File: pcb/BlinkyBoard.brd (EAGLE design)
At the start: 25.2 x 10 mm, 27 parts, among them Q1 16 MHz

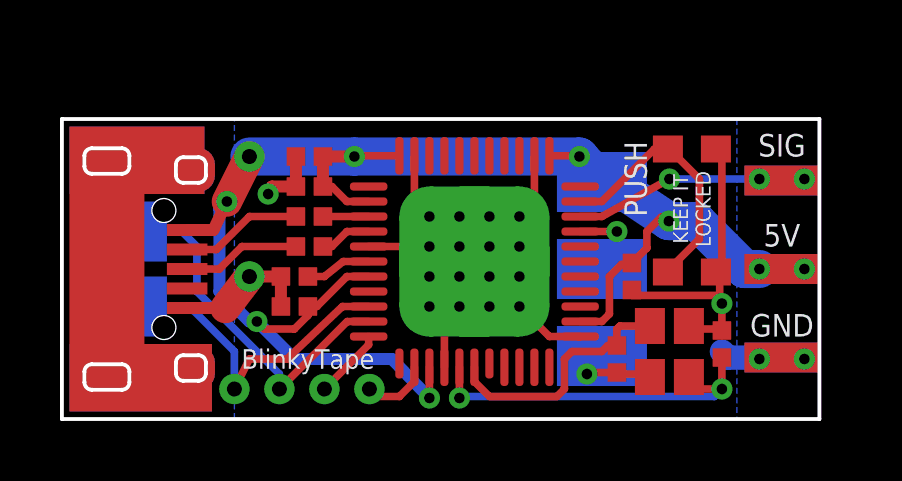
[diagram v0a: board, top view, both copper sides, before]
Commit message: Fix thru-hole micro usb pads, switch 10uF cap to 0603 package
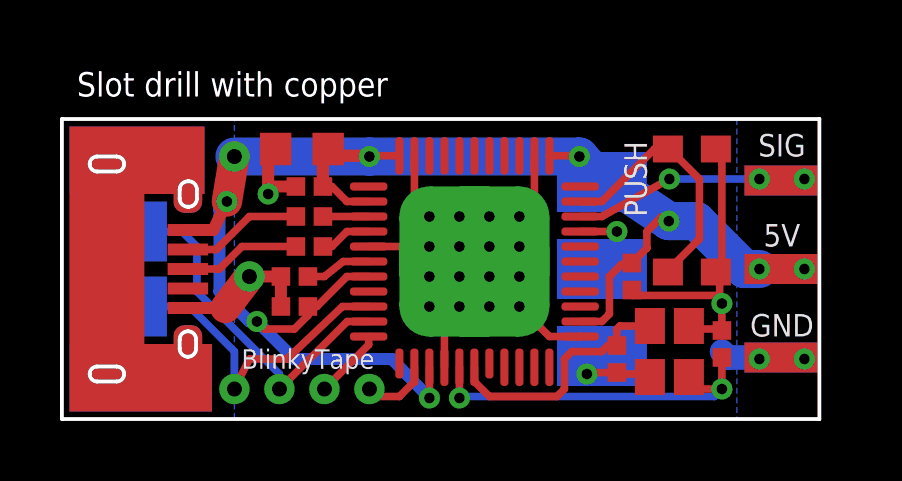
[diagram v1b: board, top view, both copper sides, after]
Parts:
- C1: device blinkiverse:CAP_0402_KEMET_MEDIAN -> adafruit:C0603K
- U$4: value MICRO_USBSMT+DIP -> MICRO_USBSMT+THRUHULE; device blinkiverse:MICRO_USB_THRUHOLE -> blinkiverse:MICRO_USB_FCI_THRUHOLE
- moved U$8 0.50 mm to (5.75, 8.75)
- moved C1 0.35 mm to (8.00, 9.00)
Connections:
- net D+_IN: now also U$4.PIN$3; no longer U$4.P$3
- net D-_IN: now also U$4.PIN$2; no longer U$4.P$2
- net GND: now also C1.2, U$4.PIN$5; no longer C1.P$2, U$4.P$5
- net VCC: now also C1.1, U$4.PIN$1; no longer C1.P$1, U$4.P$1
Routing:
- net VCC: track 54.2 -> 55.0 mm
- net GND: track 33.4 -> 34.2 mm
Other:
- board text added: "Slot drill with copper"
- board text removed: "KEEP IT LOCKED"

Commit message: Swap extra IO pads for ones that are actually Arduino pins, rename analog to A11
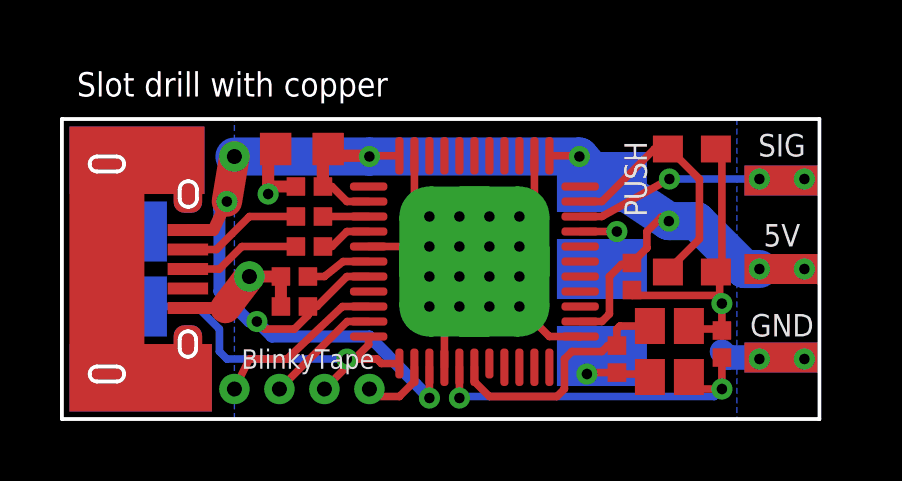
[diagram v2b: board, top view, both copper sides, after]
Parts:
- moved U$10 2.50 mm to (2.00, 6.25)
- moved U$14 2.50 mm to (2.00, 3.75)
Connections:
- net ANALOG_IN renamed A11
- new net D11: U$14.P$1, U$2.12
- new net D7: U$10.P$1, U$2.1
- net MOSI: no longer U$14.P$1
- net SCK: no longer U$10.P$1
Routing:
- net D11: track 0.00 -> 10.5 mm, vias 0 -> 1
- net MOSI: track 12.5 -> 3.90 mm
- net SCK: track 11.4 -> 5.79 mm
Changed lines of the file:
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@@
 <element name="U$8" library="blinkiverse" package="TEST_VIA_.5MM" value="TEST_VIA" x="5.75" y="8.75"/>
 <element name="WS3" library="blinkiverse" package="WS2811_CONNECTOR" value="WS2811_CONNECTOR" x="24" y="5" rot="MR0"/>
-<element name="U$10" library="blinkiverse" package="TEST_PAD_SMT" value="TEST_PAD_SMT" x="2" y="3.75" rot="MR90"/>
+<element name="U$10" library="blinkiverse" package="TEST_PAD_SMT" value="TEST_PAD_SMT" x="2" y="6.25" rot="MR90"/>
 <element name="U$11" library="blinkiverse" package="TEST_PAD_SMT" value="TEST_PAD_SMT" x="18" y="5" rot="MR90"/>
 <element name="U$12" library="blinkiverse" package="TEST_PAD_SMT" value="TEST_PAD_SMT" x="18" y="7.9" rot="MR270"/>
 <element name="U$13" library="blinkiverse" package="TEST_PAD_SMT" value="TEST_PAD_SMT" x="18" y="2.1" rot="MR270"/>
-<element name="U$14" library="blinkiverse" package="TEST_PAD_SMT" value="TEST_PAD_SMT" x="2" y="6.25" rot="MR270"/>
+<element name="U$14" library="blinkiverse" package="TEST_PAD_SMT" value="TEST_PAD_SMT" x="2" y="3.75" rot="MR270"/>
 <element name="U$15" library="blinkiverse" package="OSHW-LOGO-S" value="" x="21.25" y="6.75" rot="MR0"/>
 </elements>
@@
 <wire x1="9.51" y1="3.25" x2="10.225" y2="3.25" width="0.254" layer="1"/>
 <wire x1="9.51" y1="3.25" x2="7.25" y2="1" width="0.254" layer="1"/>
-<contactref element="U$14" pad="P$1"/>
-<wire x1="2" y1="6.25" x2="4" y2="6.25" width="0.254" layer="16"/>
-<wire x1="4" y1="6.25" x2="4.5" y2="5.75" width="0.254" layer="16"/>
-<wire x1="4.5" y1="5.75" x2="4.5" y2="4.25" width="0.254" layer="16"/>
-<wire x1="4.5" y1="4.25" x2="7.25" y2="1.5" width="0.254" layer="16"/>
-<wire x1="7.25" y1="1.5" x2="7.25" y2="1" width="0.254" layer="16"/>
 </signal>
 <signal name="MISO">
@@
 <wire x1="7.5" y1="2" x2="6.25" y2="2" width="0.254" layer="1"/>
 <wire x1="6.25" y1="2" x2="5.75" y2="1" width="0.254" layer="1"/>
-<contactref element="U$10" pad="P$1"/>
-<wire x1="2" y1="3.75" x2="4.25" y2="3.75" width="0.254" layer="16"/>
-<wire x1="4.25" y1="3.75" x2="5.75" y2="2.25" width="0.254" layer="16"/>
-<wire x1="5.75" y1="2.25" x2="5.75" y2="1" width="0.254" layer="16"/>
 </signal>
 <signal name="RST">
@@
 <wire x1="9.375" y1="5.25" x2="10.225" y2="5.25" width="0.254" layer="1"/>
 </signal>
-<signal name="ANALOG_IN">
+<signal name="A11">
 <contactref element="U$2" pad="30"/>
 <wire x1="17.275" y1="6.25" x2="18.5" y2="6.25" width="0.254" layer="1"/>
@@
 <via x="12.25" y="0.7" extent="1-16" drill="0.35"/>
 <via x="6.5" y="3.25" extent="1-16" drill="0.35"/>
-<wire x1="6.5" y1="3.25" x2="7.75" y2="2" width="0.4" layer="16"/>
-<wire x1="7.75" y1="2" x2="11" y2="2" width="0.4" layer="16"/>
-<wire x1="11" y1="2" x2="12.25" y2="0.7" width="0.4" layer="16"/>
+<wire x1="6.5" y1="3.25" x2="7" y2="2.75" width="0.4" layer="16"/>
+<wire x1="7" y1="2.75" x2="10.25" y2="2.75" width="0.4" layer="16"/>
+<wire x1="10.25" y1="2.75" x2="12.25" y2="0.7" width="0.4" layer="16"/>
 <via x="10.25" y="8.75" extent="1-16" drill="0.35"/>
 <wire x1="11.25" y1="8.775" x2="10.225" y2="8.775" width="0.254" layer="1"/>
@@
 <wire x1="18.5" y1="1.5" x2="19.5" y2="1.5" width="0.254" layer="1"/>
 </signal>
+<signal name="D11">
+<contactref element="U$2" pad="12"/>
+<contactref element="U$14" pad="P$1"/>
+<wire x1="2" y1="3.75" x2="4.5" y2="3.75" width="0.254" layer="16"/>
+<wire x1="4.5" y1="3.75" x2="5.25" y2="3" width="0.254" layer="16"/>
+<wire x1="5.25" y1="3" x2="5.25" y2="2.25" width="0.254" layer="16"/>
+<wire x1="5.25" y1="2.25" x2="5.5" y2="2" width="0.254" layer="16"/>
+<wire x1="5.5" y1="2" x2="9.5" y2="2" width="0.254" layer="16"/>
+<via x="9.5" y="2" extent="1-16" drill="0.35"/>
+<wire x1="9.5" y1="2" x2="10.5" y2="2" width="0.254" layer="1"/>
+<wire x1="11.25" y1="1.85" x2="10.65" y2="1.85" width="0.254" layer="1"/>
+<wire x1="10.65" y1="1.85" x2="10.5" y2="2" width="0.254" layer="1"/>
+</signal>
+<signal name="D7">
+<contactref element="U$2" pad="1"/>
+<contactref element="U$10" pad="P$1"/>
+<wire x1="2" y1="6.25" x2="10.225" y2="7.75" width="0" layer="19" extent="1-16"/>
+</signal>
 </signals>

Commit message: Almost have D7 squeezed in, clean up silk
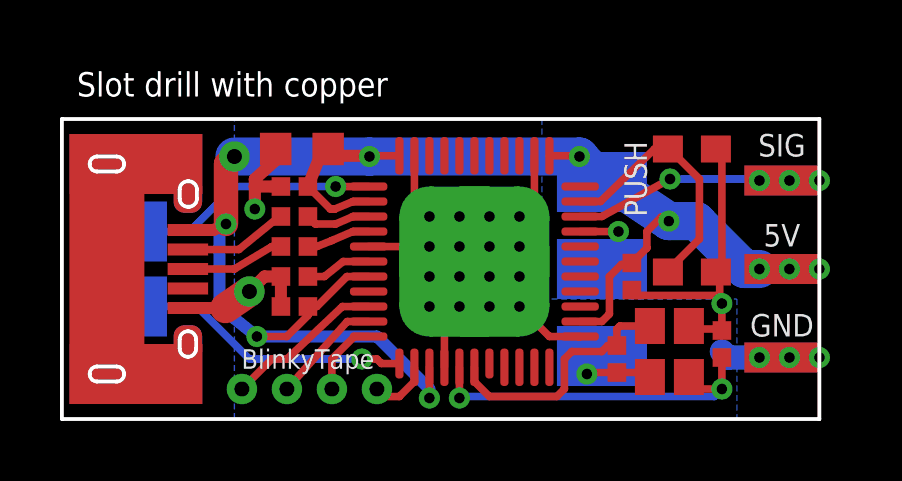
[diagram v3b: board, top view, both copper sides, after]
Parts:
- moved C2 0.50 mm to (7.75, 7.75)
- moved R1 0.50 mm to (7.75, 5.75)
- moved R2 0.50 mm to (7.75, 6.75)
- moved U$7 0.50 mm to (6.25, 4.25)
- moved U$1 0.25 mm to (9.00, 1.00)
- moved U$3 0.25 mm to (7.50, 1.00)
- moved U$5 0.25 mm to (6.00, 1.00)
- moved U$6 0.25 mm to (10.5, 1.00)
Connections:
- net GND: now also Q1.P$2, Q1.P$4
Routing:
- net D7: track 0.00 -> 8.85 mm, vias 0 -> 1
- net GND: track 34.2 -> 36.1 mm, vias 5 -> 6
- net N$1: track 1.00 -> 0.00 mm
- net D-: track 1.53 -> 2.18 mm
- net VCC: track 55.0 -> 55.6 mm, vias 8 -> 9
- net D+_IN: track 3.91 -> 3.31 mm
- net D-_IN: track 4.06 -> 3.49 mm
- net LED_DATA: track 8.68 -> 8.69 mm, vias 3 -> 4
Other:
- board text added: "5/13"
- board text added: "A11"
- board text added: "D11"
- board text added: "D7"
- board text added: "Rev D"
- board text removed: "A10"
- board text removed: "MOSI"
- board text removed: "Rev C"
- board text removed: "SCK"

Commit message: RevD candidate- Move switch to D10 (for interrupt capability), then move analog input to A10 and LED_DATA to D13.
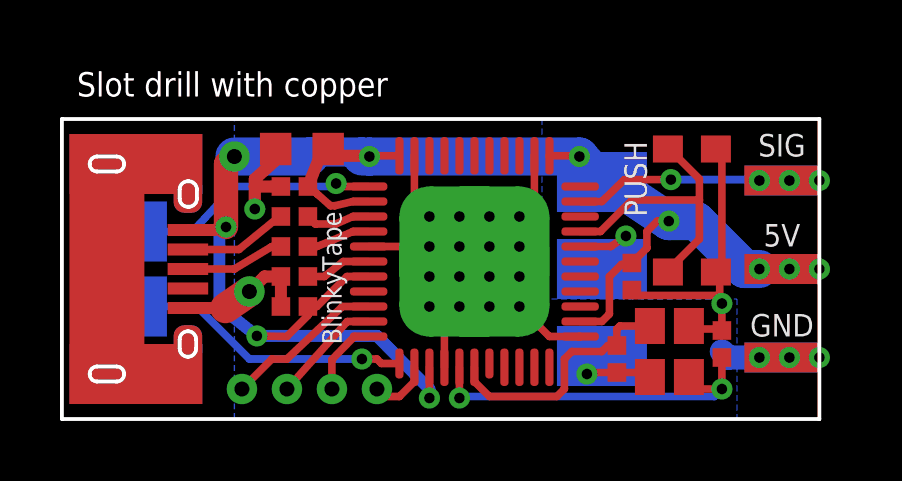
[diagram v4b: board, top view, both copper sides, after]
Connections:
- removed net A11: U$11.P$1, U$2.30
- removed net LED_DATA: U$2.31, WS1.DATA, WS3.DATA
- removed net N$10: S1.P$3, S1.P$4, U$2.32
- new net A10: U$11.P$1, U$2.29
- new net D10: S1.P$3, S1.P$4, U$2.30
- new net D13: U$2.32, WS1.DATA, WS3.DATA
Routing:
- net D10: track 0.00 -> 9.68 mm
- net N$10: track 8.90 -> 0.00 mm
- net LED_DATA: track 8.69 -> 0.00 mm, vias 4 -> 0
- net D13: track 0.00 -> 8.65 mm, vias 0 -> 4
- net A10: track 0.00 -> 3.03 mm, vias 0 -> 1
- net A11: track 2.77 -> 0.00 mm, vias 1 -> 0

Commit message: Fix copper planes under usb connector
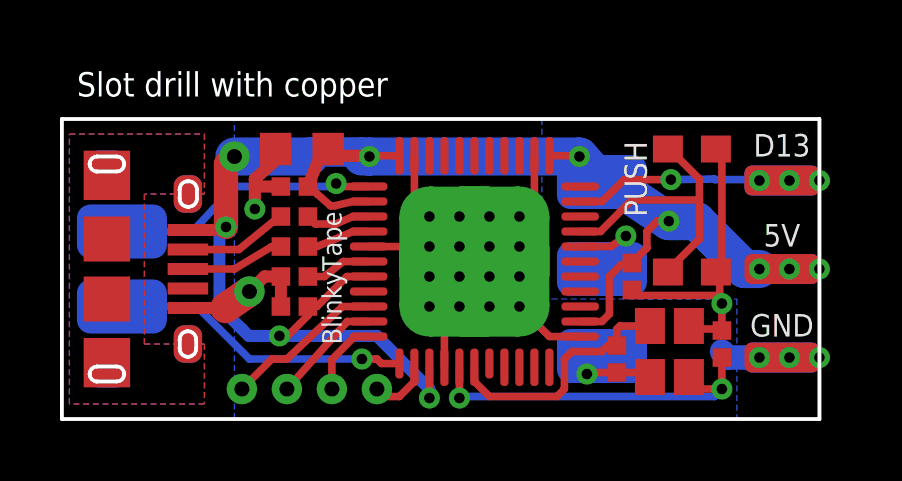
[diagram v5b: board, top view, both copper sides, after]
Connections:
- new net SHIELD: U$4.PAD$1, U$4.PAD$10, U$4.PAD$2, U$4.PAD$3, U$4.PAD$4, U$4.PAD$5, U$4.PAD$6, U$4.PAD$7, U$4.PAD$8, U$4.PAD$9
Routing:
- net VCC: track 55.7 -> 55.1 mm
- added copper zone on layer 1, net SHIELD
- added copper zone on layer 16, net SHIELD
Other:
- board text added: "D13"
- board text removed: "SIG"
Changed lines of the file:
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@@
 <grid distance="0.25" unitdist="mm" unit="mm" style="lines" multiple="1" display="no" altdistance="0.1" altunitdist="mm" altunit="mm"/>
 <layers>
-<layer number="1" name="Top" color="4" fill="1" visible="no" active="yes"/>
+<layer number="1" name="Top" color="4" fill="1" visible="yes" active="yes"/>
 <layer number="2" name="Route2" color="1" fill="3" visible="no" active="no"/>
 <layer number="3" name="Route3" color="4" fill="3" visible="no" active="no"/>
@@
 <layer number="27" name="tValues" color="7" fill="1" visible="no" active="yes"/>
 <layer number="28" name="bValues" color="7" fill="1" visible="no" active="yes"/>
-<layer number="29" name="tStop" color="7" fill="3" visible="yes" active="yes"/>
-<layer number="30" name="bStop" color="7" fill="6" visible="no" active="yes"/>
+<layer number="29" name="tStop" color="7" fill="3" visible="no" active="yes"/>
+<layer number="30" name="bStop" color="7" fill="6" visible="yes" active="yes"/>
 <layer number="31" name="tCream" color="7" fill="4" visible="no" active="yes"/>
 <layer number="32" name="bCream" color="7" fill="5" visible="no" active="yes"/>
@@
 <layer number="49" name="Reference" color="7" fill="1" visible="no" active="yes"/>
 <layer number="50" name="dxf" color="7" fill="1" visible="no" active="yes"/>
-<layer number="51" name="tDocu" color="14" fill="1" visible="no" active="yes"/>
+<layer number="51" name="tDocu" color="14" fill="1" visible="yes" active="yes"/>
 <layer number="52" name="bDocu" color="14" fill="1" visible="no" active="yes"/>
 <layer number="53" name="tGND_GNDA" color="7" fill="9" visible="no" active="no"/>
@@
 Tape</text>
 <text x="8.75" y="3.85" size="0.8128" layer="26" font="vector" ratio="20" rot="MR0" align="center">Rev D</text>
-<text x="24" y="8.75" size="0.75" layer="25" font="vector" ratio="15" align="bottom-center">SIG</text>
+<text x="24" y="8.75" size="0.75" layer="25" font="vector" ratio="15" align="bottom-center">D13</text>
 <text x="24" y="5.75" size="0.75" layer="25" font="vector" ratio="15" align="bottom-center">5V</text>
 <text x="24" y="2.75" size="0.75" layer="25" font="vector" ratio="15" align="bottom-center">GND</text>
@@
 <text x="9" y="4.7" size="0.65" layer="25" font="vector" ratio="15" rot="R90" align="center">BlinkyTape</text>
 <text x="10.75" y="2.5" size="0.9" layer="26" font="vector" ratio="20" rot="MR0" align="center">blinkytape.com</text>
-<rectangle x1="0.25" y1="7.5" x2="4.68" y2="9.5" layer="16"/>
-<rectangle x1="0.25" y1="0.5" x2="4.68" y2="2.5" layer="16"/>
-<rectangle x1="0.25" y1="0.5" x2="4.68" y2="2.5" layer="1"/>
-<rectangle x1="0.25" y1="7.5" x2="4.68" y2="9.5" layer="1"/>
-<rectangle x1="0.25" y1="2.5" x2="2.75" y2="7.5" layer="1"/>
-<text x="24" y="8.75" size="0.75" layer="26" font="vector" ratio="15" rot="MR0" align="bottom-center">SIG</text>
+<text x="24" y="8.75" size="0.75" layer="26" font="vector" ratio="15" rot="MR0" align="bottom-center">D13</text>
 <text x="24" y="5.75" size="0.75" layer="26" font="vector" ratio="15" rot="MR0" align="bottom-center">5V</text>
 <text x="24" y="2.75" size="0.75" layer="26" font="vector" ratio="15" rot="MR0" align="bottom-center">GND</text>
@@
 <via x="25.25" y="7.95" extent="1-16" drill="0.35"/>
 <wire x1="24.25" y1="7.95" x2="25.25" y2="7.95" width="0.254" layer="16"/>
-<wire x1="20.3" y1="7.98" x2="23.2" y2="7.98" width="0.254" layer="16"/>
+<wire x1="20.3" y1="7.98" x2="21.75" y2="8" width="0.254" layer="16"/>
+<wire x1="21.75" y1="8" x2="21.77" y2="7.98" width="0.254" layer="16"/>
+<wire x1="21.77" y1="7.98" x2="23.2" y2="7.98" width="0.254" layer="16"/>
 <wire x1="23.2" y1="7.98" x2="23.25" y2="7.95" width="0.254" layer="16"/>
 <contactref element="U$2" pad="32"/>
@@
 <wire x1="12.25" y1="1.725" x2="12.25" y2="0.7" width="0.254" layer="1"/>
 <via x="12.25" y="0.7" extent="1-16" drill="0.35"/>
-<via x="6.5" y="2.77" extent="1-16" drill="0.35"/>
-<wire x1="6.5" y1="2.77" x2="10.5" y2="2.77" width="0.4" layer="16"/>
+<via x="7.25" y="2.77" extent="1-16" drill="0.35"/>
+<wire x1="7.25" y1="2.77" x2="10.5" y2="2.77" width="0.4" layer="16"/>
 <wire x1="10.5" y1="2.77" x2="12.25" y2="1" width="0.4" layer="16"/>
 <wire x1="12.25" y1="1" x2="12.25" y2="0.7" width="0.4" layer="16"/>
@@
 <wire x1="5.47" y1="8.5" x2="5.75" y2="8.75" width="0.8128" layer="1"/>
 <via x="5.47" y="6.4" extent="1-16" drill="0.35"/>
-<wire x1="6.5" y1="2.77" x2="5.25" y2="3.75" width="0.4" layer="16"/>
+<wire x1="7.25" y1="2.77" x2="6.23" y2="2.77" width="0.4" layer="16"/>
+<wire x1="6.23" y1="2.77" x2="6" y2="3" width="0.4" layer="16"/>
+<wire x1="6" y1="3" x2="5.25" y2="3.75" width="0.4" layer="16"/>
 <wire x1="5.25" y1="3.75" x2="5.25" y2="6.25" width="0.4" layer="16"/>
 <wire x1="5.25" y1="6.25" x2="5.47" y2="6.4" width="0.4" layer="16"/>
@@
 <wire x1="8.2" y1="3.75" x2="8.2" y2="3.45" width="0.254" layer="1"/>
 <wire x1="8.2" y1="3.45" x2="7.5" y2="2.75" width="0.254" layer="1"/>
-<wire x1="7.5" y1="2.75" x2="6.5" y2="2.77" width="0.254" layer="1"/>
+<wire x1="7.5" y1="2.75" x2="7.25" y2="2.77" width="0.254" layer="1"/>
 <wire x1="20.23076875" y1="6.596153125" x2="21.153846875" y2="6.596153125" width="1.27" layer="16"/>
 <wire x1="8.875" y1="9" x2="8.7" y2="9" width="0.4064" layer="1"/>
@@
 <wire x1="18.3" y1="5.75" x2="18.8" y2="6.1" width="0.254" layer="1"/>
 </signal>
+<signal name="SHIELD">
+<contactref element="U$4" pad="PAD$8"/>
+<contactref element="U$4" pad="PAD$10"/>
+<contactref element="U$4" pad="PAD$2"/>
+<contactref element="U$4" pad="PAD$4"/>
+<contactref element="U$4" pad="PAD$5"/>
+<contactref element="U$4" pad="PAD$7"/>
+<contactref element="U$4" pad="PAD$6"/>
+<contactref element="U$4" pad="PAD$1"/>
+<contactref element="U$4" pad="PAD$3"/>
+<contactref element="U$4" pad="PAD$9"/>
+<polygon width="0.254" layer="1">
+<vertex x="0.25" y="9.5"/>
+<vertex x="4.75" y="9.5"/>
+<vertex x="4.75" y="7.5"/>
+<vertex x="2.75" y="7.5"/>
+<vertex x="2.75" y="2.5"/>
+<vertex x="4.75" y="2.5"/>
+<vertex x="4.75" y="0.5"/>
+<vertex x="0.25" y="0.5"/>
+</polygon>
+<polygon width="0.254" layer="16" isolate="0.254">
+<vertex x="0.25" y="9.5"/>
+<vertex x="4.75" y="9.5"/>
+<vertex x="4.75" y="7.5"/>
+<vertex x="2.75" y="7.5"/>
+<vertex x="2.75" y="2.5"/>
+<vertex x="4.75" y="2.5"/>
+<vertex x="4.75" y="0.5"/>
+<vertex x="0.25" y="0.5"/>
+</polygon>
+<wire x1="4.2" y1="2.5" x2="4.2" y2="2.5" width="0" layer="19" extent="1-16"/>
+<wire x1="4.2" y1="7.5" x2="4.2" y2="7.5" width="0" layer="19" extent="1-16"/>
+</signal>
 </signals>

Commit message: PCB design fix: add cream to all USB ground pads!
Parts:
- WS1, WS3: value WS2811_CONNECTOR -> WS2811_CONNECTORSTRIP
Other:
- board text added: "Rev Exx"
- board text removed: "Rev D"
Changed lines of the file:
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@@
 <layer number="27" name="tValues" color="7" fill="1" visible="no" active="yes"/>
 <layer number="28" name="bValues" color="7" fill="1" visible="no" active="yes"/>
-<layer number="29" name="tStop" color="7" fill="3" visible="no" active="yes"/>
+<layer number="29" name="tStop" color="7" fill="3" visible="yes" active="yes"/>
 <layer number="30" name="bStop" color="7" fill="6" visible="yes" active="yes"/>
 <layer number="31" name="tCream" color="7" fill="4" visible="no" active="yes"/>
@@
 <text x="8.75" y="6" size="1.016" layer="26" font="vector" ratio="20" rot="MR0" align="center">Blinky
 Tape</text>
-<text x="8.75" y="3.85" size="0.8128" layer="26" font="vector" ratio="20" rot="MR0" align="center">Rev D</text>
+<text x="8.75" y="3.85" size="0.8128" layer="26" font="vector" ratio="20" rot="MR0" align="center">Rev Exx</text>
 <text x="24" y="8.75" size="0.75" layer="25" font="vector" ratio="15" align="bottom-center">D13</text>
 <text x="24" y="5.75" size="0.75" layer="25" font="vector" ratio="15" align="bottom-center">5V</text>
@@
 <element name="Q1" library="blinkiverse" package="CRSYTAL_2520" value="16 MHz" x="20.25" y="2.25" smashed="yes" rot="R270"/>
 <element name="C4" library="blinkiverse" package="CAP_0402_KEMET_MEDIAN" value="0.1uF" x="19" y="4.75" smashed="yes" rot="R270"/>
-<element name="WS1" library="blinkiverse" package="WS2811_CONNECTOR" value="WS2811_CONNECTOR" x="24" y="5"/>
+<element name="WS1" library="blinkiverse" package="WS2811_CONNECTOR" value="WS2811_CONNECTORSTRIP" x="24" y="5"/>
 <element name="U$4" library="blinkiverse" package="MICRO_USB_FCI_THRUHOLE" value="MICRO_USBSMT+THRUHULE" x="1.5" y="5" rot="R270"/>
 <element name="U$1" library="blinkiverse" package="TEST_VIA_.5MM" value="TEST_VIA" x="9" y="1"/>
@@
 <element name="U$7" library="blinkiverse" package="TEST_VIA_.5MM" value="TEST_VIA" x="6.25" y="4.25"/>
 <element name="U$8" library="blinkiverse" package="TEST_VIA_.5MM" value="TEST_VIA" x="5.75" y="8.75"/>
-<element name="WS3" library="blinkiverse" package="WS2811_CONNECTOR" value="WS2811_CONNECTOR" x="24" y="5" rot="MR0"/>
+<element name="WS3" library="blinkiverse" package="WS2811_CONNECTOR" value="WS2811_CONNECTORSTRIP" x="24" y="5" rot="MR0"/>
 <element name="U$10" library="blinkiverse" package="TEST_PAD_SMT" value="TEST_PAD_SMT" x="2" y="6.25" rot="MR90"/>
 <element name="U$11" library="blinkiverse" package="TEST_PAD_SMT" value="TEST_PAD_SMT" x="18" y="5" rot="MR90"/>
